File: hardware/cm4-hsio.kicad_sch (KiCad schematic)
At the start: 1 part, among them J1 DF40C-100DP-0.4V_51_

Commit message: Adding SDRAM - missing 3 pins
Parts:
- J1: footprint apparillo-lib:HRS_DF40C-100DP-0.4V_51_ -> ulx5m-gs:HRS_DF40C-100DP-0.4V_51_
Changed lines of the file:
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@@
 			)
 		)
-		(property "Footprint" "apparillo-lib:HRS_DF40C-100DP-0.4V_51_"
+		(property "Footprint" "ulx5m-gs:HRS_DF40C-100DP-0.4V_51_"
 			(at 152.4 88.9 0)
 			(effects

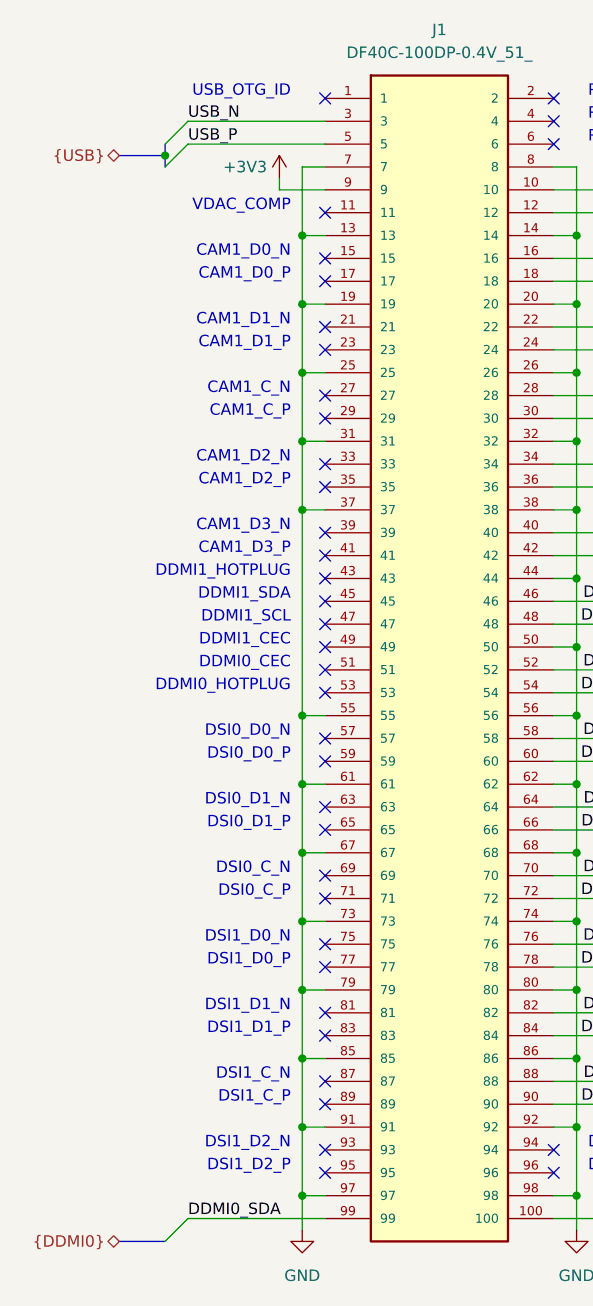
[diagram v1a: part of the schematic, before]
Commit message: Adding USB connector and level converter
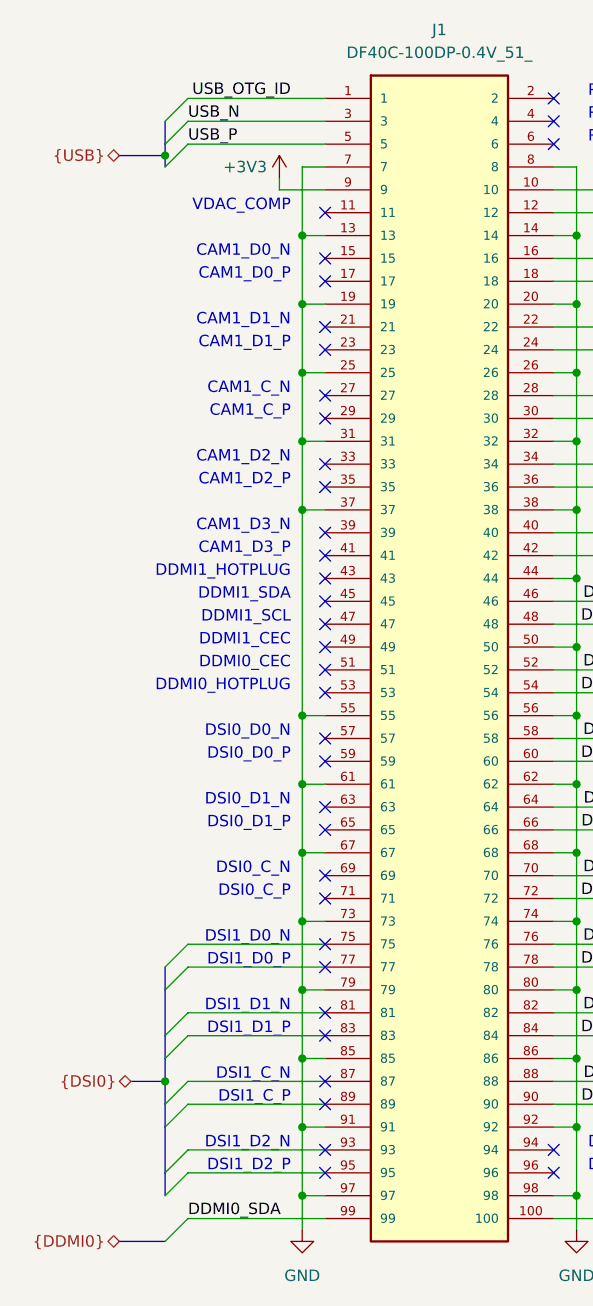
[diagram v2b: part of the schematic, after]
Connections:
- net USB_OTG_ID: now reaches J1.1
- no-connect marks 37 -> 36
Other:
- note removed: "USB_OTG_ID"

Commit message: Routing diff clock
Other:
- company: (none) -> ${project_creator}
- title: (none) -> ${project_name}
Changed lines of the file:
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@@
 	(generator_version "9.0")
 	(paper "A4")
+	(title_block
+		(title "${project_name}")
+		(date "2025-06-24")
+		(rev "${project_version}")
+		(company "${project_creator}")
+		(comment 1 "${project_license}")
+	)
 	(bus_alias "CAM0"
 		(members "CAM0_D0_P" "CAM0_D0_N" "CAM0_D1_P" "CAM0_D1_N" "CAM0_D2_P" "CAM0_D2_N"

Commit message: Updat to CM5
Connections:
- net +3V3: no longer names the net of J1.9
- net CAM0_C_N renamed USB3_0_C_N
- net CAM0_C_P renamed USB3_0_C_P
- net CAM0_D0_N renamed USB3_0_D0_N
- net CAM0_D0_P renamed USB3_0_D0_P
- net CAM0_D1_N renamed USB3_0_D1_N
- net CAM0_D1_P renamed USB3_0_D1_P
- no-connect marks 36 -> 25
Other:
- note added: "DDMI0"
- note added: "DDMI1"
- note added: "DDMI1_HP"
- note added: "DDMI_SE"
- note added: "MIPI0"
- note added: "MIPI0_C_N"
- note added: "MIPI0_C_P"
- note added: "MIPI0_D0_N"
- note added: "MIPI0_D0_P"
- note added: "MIPI0_D1_N"
- note added: "MIPI0_D1_P"
- note added: "MIPI0_D2_N"
- note added: "MIPI0_D2_P"
- note added: "MIPI0_D3_N"
- note added: "MIPI0_D3_P"
- note added: "MIPI1"
- note added: "MIPI1_C_N"
- note added: "MIPI1_C_P"
- note added: "MIPI1_D0_N"
- note added: "MIPI1_D0_P"
- note added: "MIPI1_D1_N"
- note added: "MIPI1_D1_P"
- note added: "MIPI1_D2_N"
- note added: "MIPI1_D2_P"
- note added: "MIPI1_D3_N"
- note added: "MIPI1_D3_P"
- note added: "PCIe"
- note added: "PCIe_PWR_EN"
- note added: "PCIe_nWAKE"
- note added: "PCInRES"
- note added: "USB"
- note added: "USB3_0"
- note added: "USB3_1"
- note added: "VBUS_EN"
- note removed: "CAM1_C_N"
- note removed: "CAM1_C_P"
- note removed: "CAM1_D0_N"
- note removed: "CAM1_D0_P"
- note removed: "CAM1_D1_N"
- note removed: "CAM1_D1_P"
- note removed: "CAM1_D2_N"
- note removed: "CAM1_D2_P"
- note removed: "CAM1_D3_N"
- note removed: "CAM1_D3_P"
- note removed: "DDMI1_HOTPLUG"
- note removed: "DSI1_C_N"
- note removed: "DSI1_C_P"
- note removed: "DSI1_D0_N"
- note removed: "DSI1_D0_P"
- note removed: "DSI1_D1_N"
- note removed: "DSI1_D1_P"
- note removed: "DSI1_D2_N"
- note removed: "DSI1_D2_P"
- note removed: "DSI1_D3_N"
- note removed: "DSI1_D3_P"
- note removed: "Reserved"
- note removed: "VDAC_COMP"

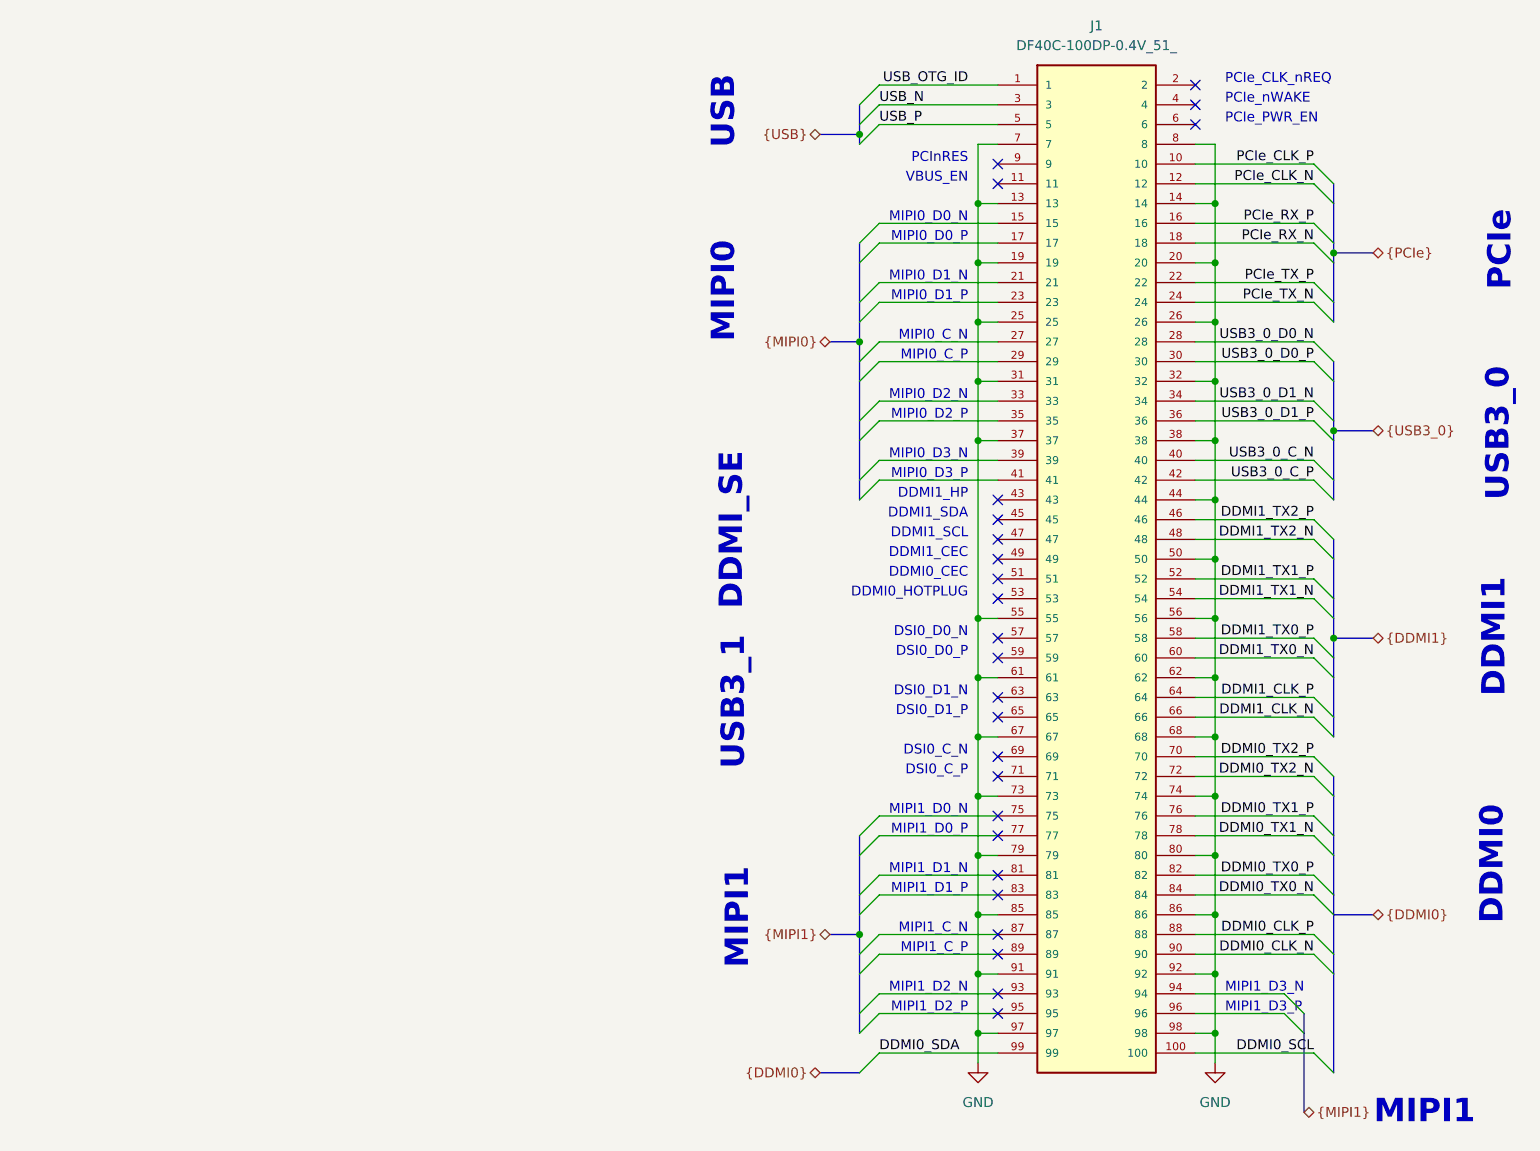
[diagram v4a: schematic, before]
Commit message: Clearing ERC errors/warnings
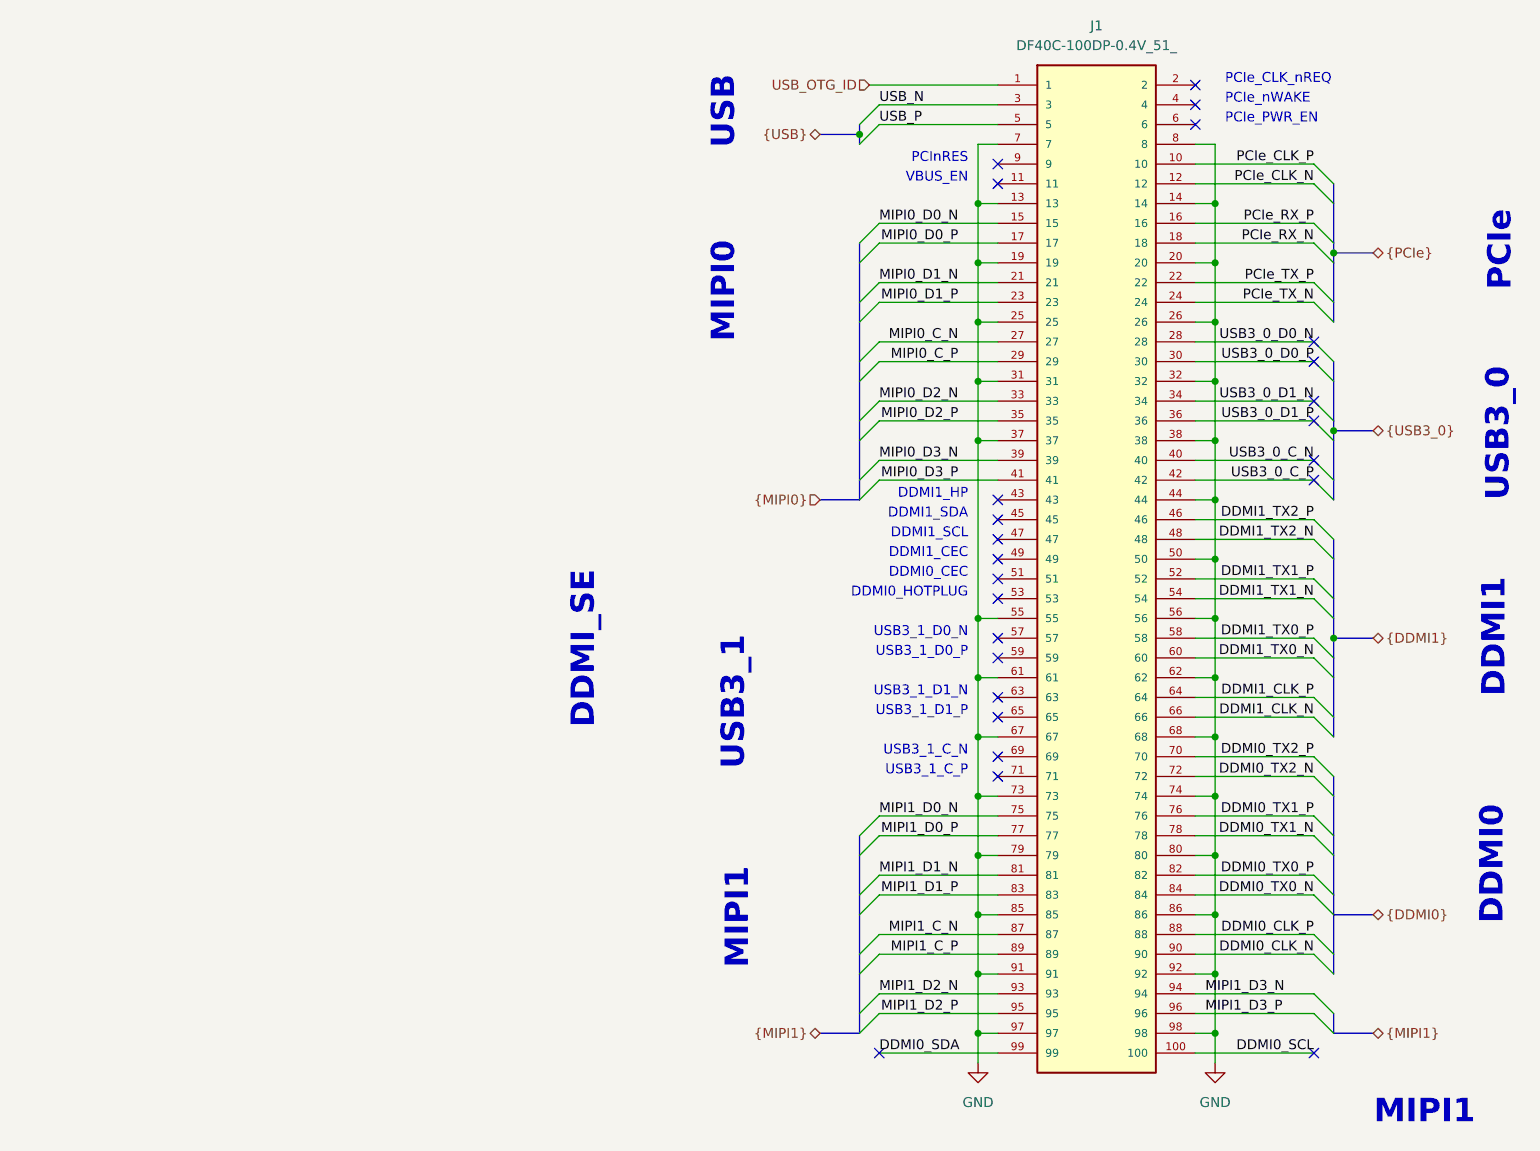
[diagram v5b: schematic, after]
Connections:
- net MIPI0_D0_N: now reaches J1.15
- net MIPI0_D0_P: now reaches J1.17
- net MIPI0_D1_N: now reaches J1.21
- net MIPI0_D1_P: now reaches J1.23
- net MIPI0_C_N: now reaches J1.27
- net MIPI0_C_P: now reaches J1.29
- net MIPI0_D2_N: now reaches J1.33
- net MIPI0_D2_P: now reaches J1.35
- net MIPI0_D3_N: now reaches J1.39
- net MIPI0_D3_P: now reaches J1.41
- net MIPI1_D0_N: now reaches J1.75
- net MIPI1_D0_P: now reaches J1.77
- net MIPI1_D1_N: now reaches J1.81
- net MIPI1_D1_P: now reaches J1.83
- net MIPI1_C_N: now reaches J1.87
- net MIPI1_C_P: now reaches J1.89
- net MIPI1_D2_N: now reaches J1.93
- net MIPI1_D3_N: now reaches J1.94
- net MIPI1_D2_P: now reaches J1.95
- net MIPI1_D3_P: now reaches J1.96
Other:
- note added: "USB3_1_C_N"
- note added: "USB3_1_C_P"
- note added: "USB3_1_D0_N"
- note added: "USB3_1_D0_P"
- note added: "USB3_1_D1_N"
- note added: "USB3_1_D1_P"
- note removed: "DSI0_C_N"
- note removed: "DSI0_C_P"
- note removed: "DSI0_D0_N"
- note removed: "DSI0_D0_P"
- note removed: "DSI0_D1_N"
- note removed: "DSI0_D1_P"
- note removed: "MIPI0_C_N"
- note removed: "MIPI0_C_P"
- note removed: "MIPI0_D0_N"
- note removed: "MIPI0_D0_P"
- note removed: "MIPI0_D1_N"
- note removed: "MIPI0_D1_P"
- note removed: "MIPI0_D2_N"
- note removed: "MIPI0_D2_P"
- note removed: "MIPI0_D3_N"
- note removed: "MIPI0_D3_P"
- note removed: "MIPI1_C_N"
- note removed: "MIPI1_C_P"
- note removed: "MIPI1_D0_N"
- note removed: "MIPI1_D0_P"
- note removed: "MIPI1_D1_N"
- note removed: "MIPI1_D1_P"
- note removed: "MIPI1_D2_N"
- note removed: "MIPI1_D2_P"
- note removed: "MIPI1_D3_N"
- note removed: "MIPI1_D3_P"
